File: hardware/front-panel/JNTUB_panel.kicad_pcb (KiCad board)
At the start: 2 copper layers, 20.3 x 128.5 mm, 0 parts

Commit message: [JNTUB-HW] Finish v0.1 of front panel
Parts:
- added REF**: MountingHole_8.4mm_M8, Mounting_Holes:MountingHole_8.4mm_M8, F.Cu at (94.6, 160.6)
- added REF**: MountingHole_8.4mm_M8, Mounting_Holes:MountingHole_8.4mm_M8, F.Cu at (102.4, 109.5)
- added REF**: MountingHole_8.4mm_M8, Mounting_Holes:MountingHole_8.4mm_M8, F.Cu at (92.2, 109.5)
- added REF**: MountingHole_8.4mm_M8, Mounting_Holes:MountingHole_8.4mm_M8, F.Cu at (97.3, 93.0)
- added REF**: MountingHole_8.4mm_M8, Mounting_Holes:MountingHole_8.4mm_M8, F.Cu at (97.3, 72.6)
- added REF**: MountingHole_8.4mm_M8, Mounting_Holes:MountingHole_8.4mm_M8, F.Cu at (97.3, 52.3)
- added REF**: MountingHole_8.4mm_M8, Mounting_Holes:MountingHole_8.4mm_M8, F.Cu at (94.6, 38.0)
- added REF**: MountingHole_8.4mm_M8, Mounting_Holes:MountingHole_8.4mm_M8, F.Cu at (97.3, 147.6)
- added REF**: MountingHole_8.4mm_M8, Mounting_Holes:MountingHole_8.4mm_M8, F.Cu at (97.3, 143.8)
- added REF**: MountingHole_8.4mm_M8, Mounting_Holes:MountingHole_8.4mm_M8, F.Cu at (97.3, 118.1)
- added REF**: MountingHole_8.4mm_M8, Mounting_Holes:MountingHole_8.4mm_M8, F.Cu at (102.4, 137.2)
- added REF**: MountingHole_8.4mm_M8, Mounting_Holes:MountingHole_8.4mm_M8, F.Cu at (92.2, 137.2)
- added REF**: MountingHole_8.4mm_M8, Mounting_Holes:MountingHole_8.4mm_M8, F.Cu at (92.2, 124.7)
- added REF**: MountingHole_8.4mm_M8, Mounting_Holes:MountingHole_8.4mm_M8, F.Cu at (102.4, 124.7)
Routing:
- net (no net): track 0.00 -> 130.5 mm
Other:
- board size 20.3 x 128.5 mm -> 20.1 x 128.5 mm
- board text added: "1 2 3 4 5 6 7 8 9 0"
- board text added: "CLK/ TRG"
- board text added: "DITTO"
- board text added: "JLCJLCJLCJLC"
- board text added: "JNTUB"
- board text added: "OUT"
- board text added: "TEST"
- board text added: "test"

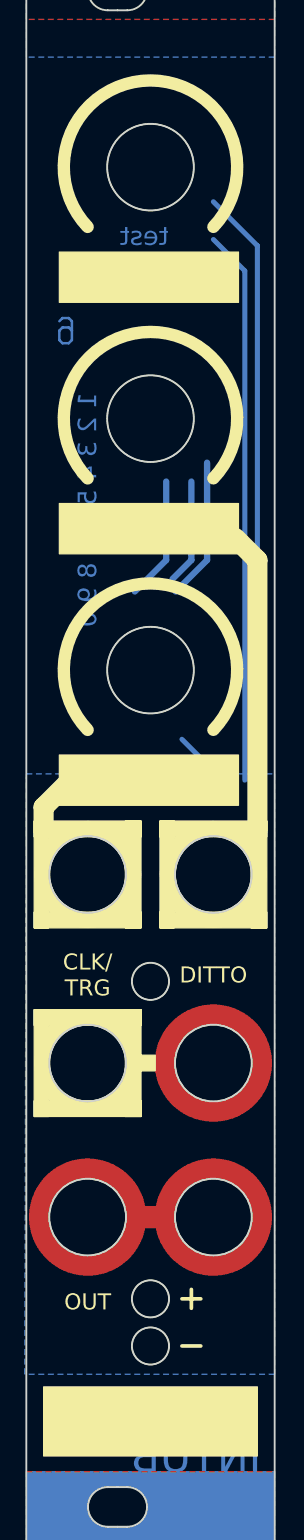
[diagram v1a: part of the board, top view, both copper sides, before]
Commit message: [JNTUB-HW] JNTUB Hardware Revision 0.2
* Add resistor to drain C12 (PWM filter cap)
* Add optional parallel resistor to PWM filter
  * selectable by jumper
  * increases the cutoff frequency to audio range
* Add resistor between 5V and MCU RESET to allow for ISP
* Move a few resistors to Board 1
* Add ISP programming headers!
* Change all resistors and diodes to standing
* Shorten pin headers that connect Boards 1 and 2
* Ditch ground pour on Board 1 in favor of direct traces
* Move CV 1 and CV 2 jacks down a bit
* Slightly adjust LED positions
* Adjust front panel to match moved components
* Tweak design of front panel
* Fix up some 3D models
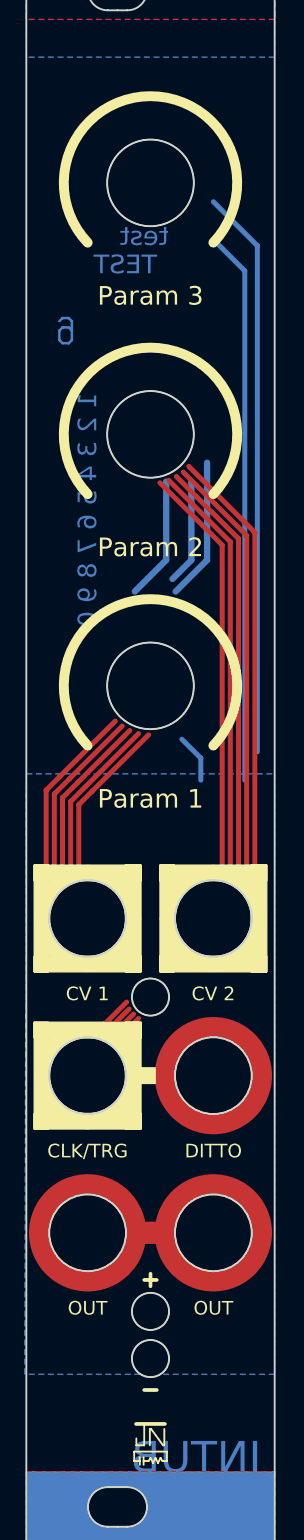
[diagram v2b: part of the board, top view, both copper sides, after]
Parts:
- removed the REF** at (102.4, 109.5)
- removed the REF** at (92.2, 109.5)
- removed the REF** at (97.3, 93.0)
- removed the REF** at (97.3, 72.6)
- removed the REF** at (97.3, 52.3)
- removed the REF** at (97.3, 147.6)
- removed the REF** at (97.3, 143.8)
- removed the REF** at (97.3, 118.1)
- removed the REF** at (102.4, 137.2)
- removed the REF** at (92.2, 137.2)
- removed the REF** at (92.2, 124.7)
- removed the REF** at (102.4, 124.7)
- added REF**: MountingHole_8.4mm_M8, Mounting_Holes:MountingHole_8.4mm_M8, F.Cu at (102.4, 113.0)
- added REF**: MountingHole_8.4mm_M8, Mounting_Holes:MountingHole_8.4mm_M8, F.Cu at (92.2, 113.0)
- added REF**: MountingHole_8.4mm_M8, Mounting_Holes:MountingHole_8.4mm_M8, F.Cu at (97.3, 94.2)
- added REF**: MountingHole_8.4mm_M8, Mounting_Holes:MountingHole_8.4mm_M8, F.Cu at (97.3, 73.9)
- added REF**: MountingHole_8.4mm_M8, Mounting_Holes:MountingHole_8.4mm_M8, F.Cu at (97.3, 53.6)
- added REF**: MountingHole_8.4mm_M8, Mounting_Holes:MountingHole_8.4mm_M8, F.Cu at (97.3, 148.6)
- added REF**: MountingHole_8.4mm_M8, Mounting_Holes:MountingHole_8.4mm_M8, F.Cu at (97.3, 144.8)
- added REF**: MountingHole_8.4mm_M8, Mounting_Holes:MountingHole_8.4mm_M8, F.Cu at (97.3, 119.4)
- added REF**: MountingHole_8.4mm_M8, Mounting_Holes:MountingHole_8.4mm_M8, F.Cu at (102.4, 138.4)
- added REF**: MountingHole_8.4mm_M8, Mounting_Holes:MountingHole_8.4mm_M8, F.Cu at (92.2, 138.4)
- added REF**: MountingHole_8.4mm_M8, Mounting_Holes:MountingHole_8.4mm_M8, F.Cu at (92.2, 125.7)
- added REF**: MountingHole_8.4mm_M8, Mounting_Holes:MountingHole_8.4mm_M8, F.Cu at (102.4, 125.7)
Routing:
- net (no net): track 130.5 -> 393.8 mm
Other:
- outline, holes or cut-outs redrawn
- net class Default: clearance 0.3048 -> 0.1524
- rule trace_clearance: 0.3048 -> 0.1524
- board text added: "CLK/TRG"
- board text added: "CV 1"
- board text added: "CV 2"
- board text added: "Param 1"
- board text added: "Param 2"
- board text added: "Param 3"
- board text removed: "CLK/ TRG"

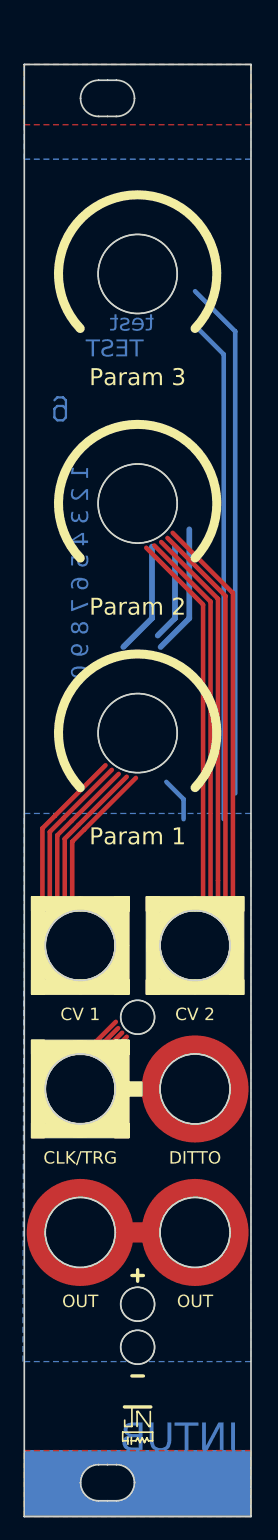
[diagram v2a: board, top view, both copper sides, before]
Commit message: [JNTUB-HW] Shift panel holes down a bit
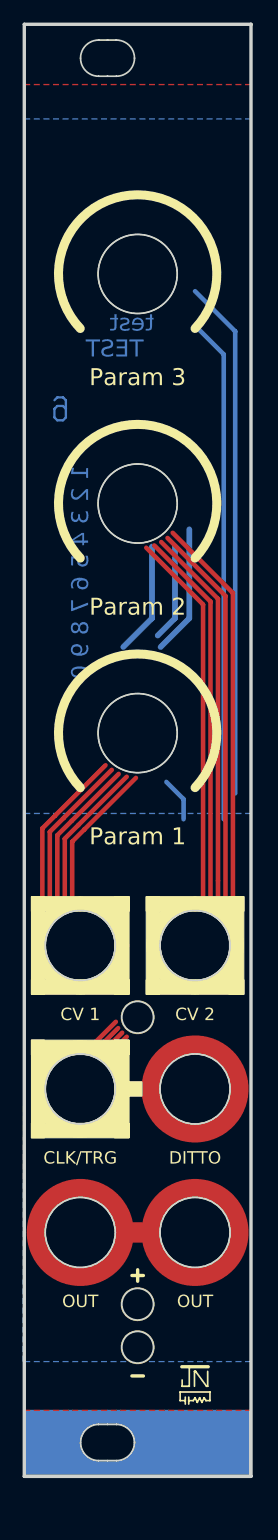
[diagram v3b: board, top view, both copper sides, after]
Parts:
- moved REF** 3.57 mm to (94.6, 34.5)
- moved REF** 3.54 mm to (94.6, 157.0)
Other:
- outline, holes or cut-outs redrawn
- board text added: "At least 0.45 in"
- board text added: "Jack Circular Nut Diameter"
- board text added: "Jack Drill Hole"
- board text added: "Knob Diameter"
- board text added: "LED Drill Hole"
- board text added: "Potentiometer Drill Hole"
